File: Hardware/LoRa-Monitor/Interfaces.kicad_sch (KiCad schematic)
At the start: 37 parts, among them Q1 ZXTN25100DFH, Q2 ZXTN25100DFH, Q3 ZXTN25100DFH, Q4 ZXTN25100DFH, Q5 ZXTN25100DFH, Q6 ZXTN25100DFH, U1 ACPL-M61L, U2 ACPL-M61L, U3 ACPL-M61L, U4 MAX3483, U5 ACPL-M61L, U6 ACPL-M61L, U7 ACPL-M61L

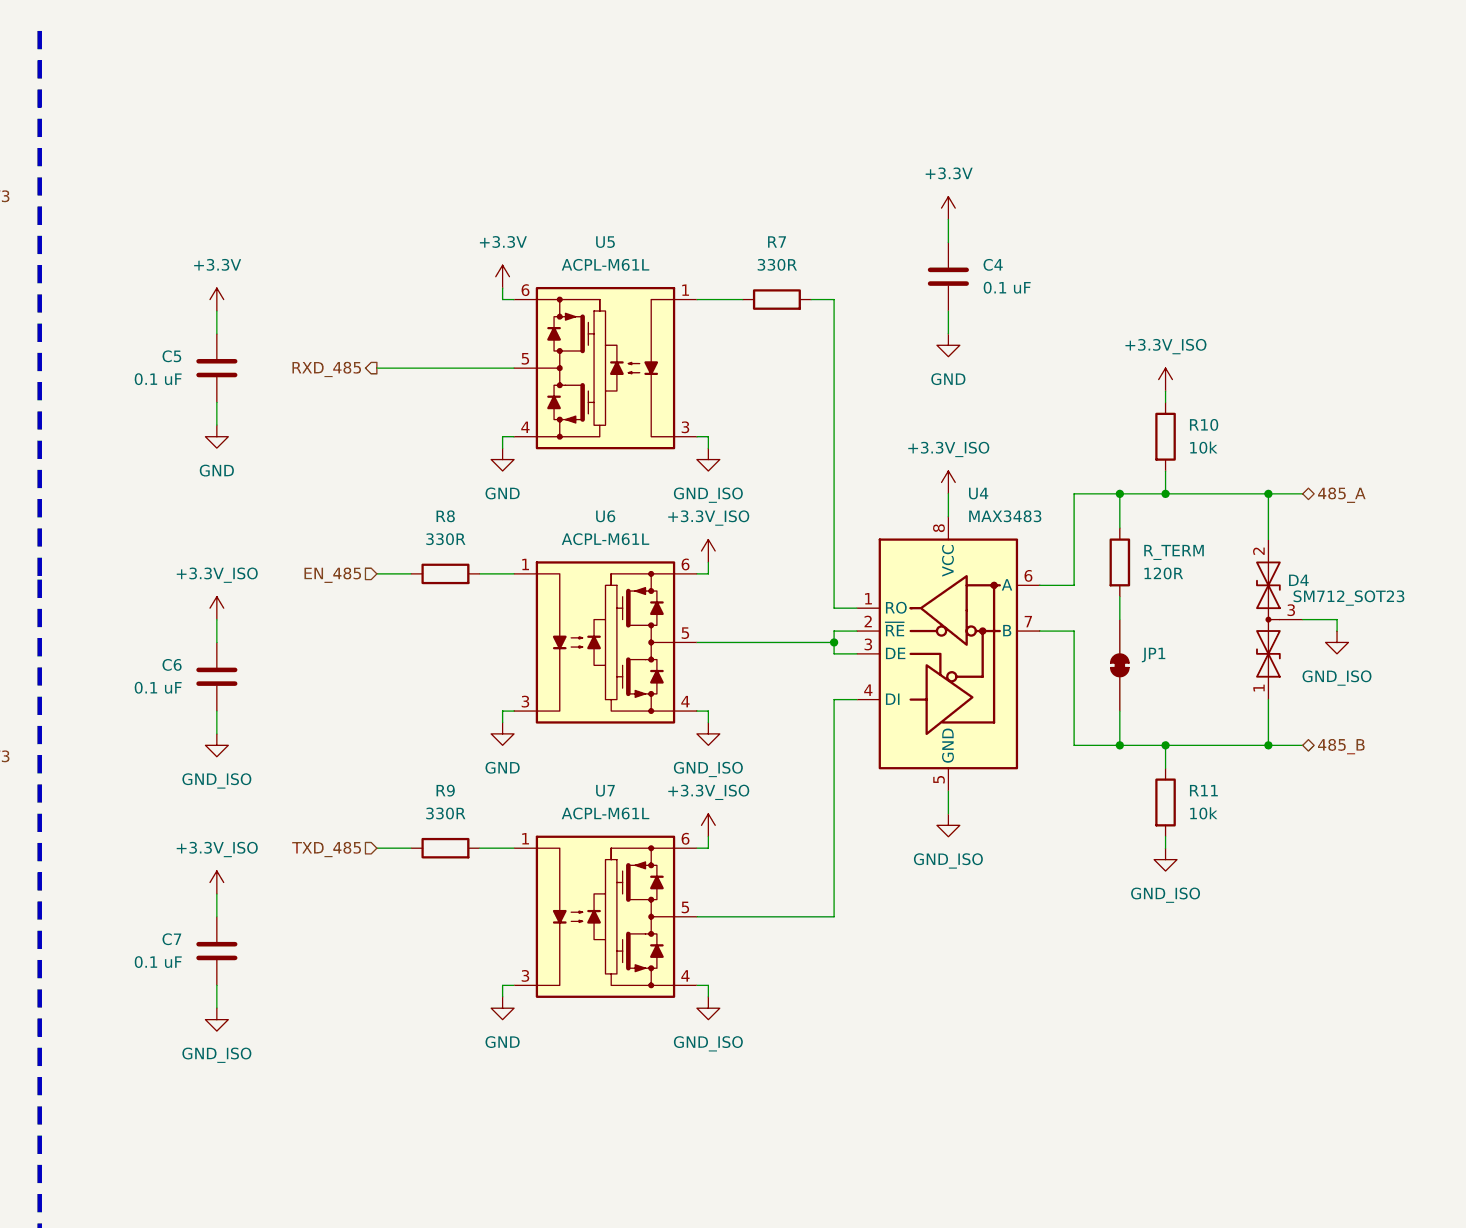
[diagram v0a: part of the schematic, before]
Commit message: Fixed Power and Ground on the Interface nodes
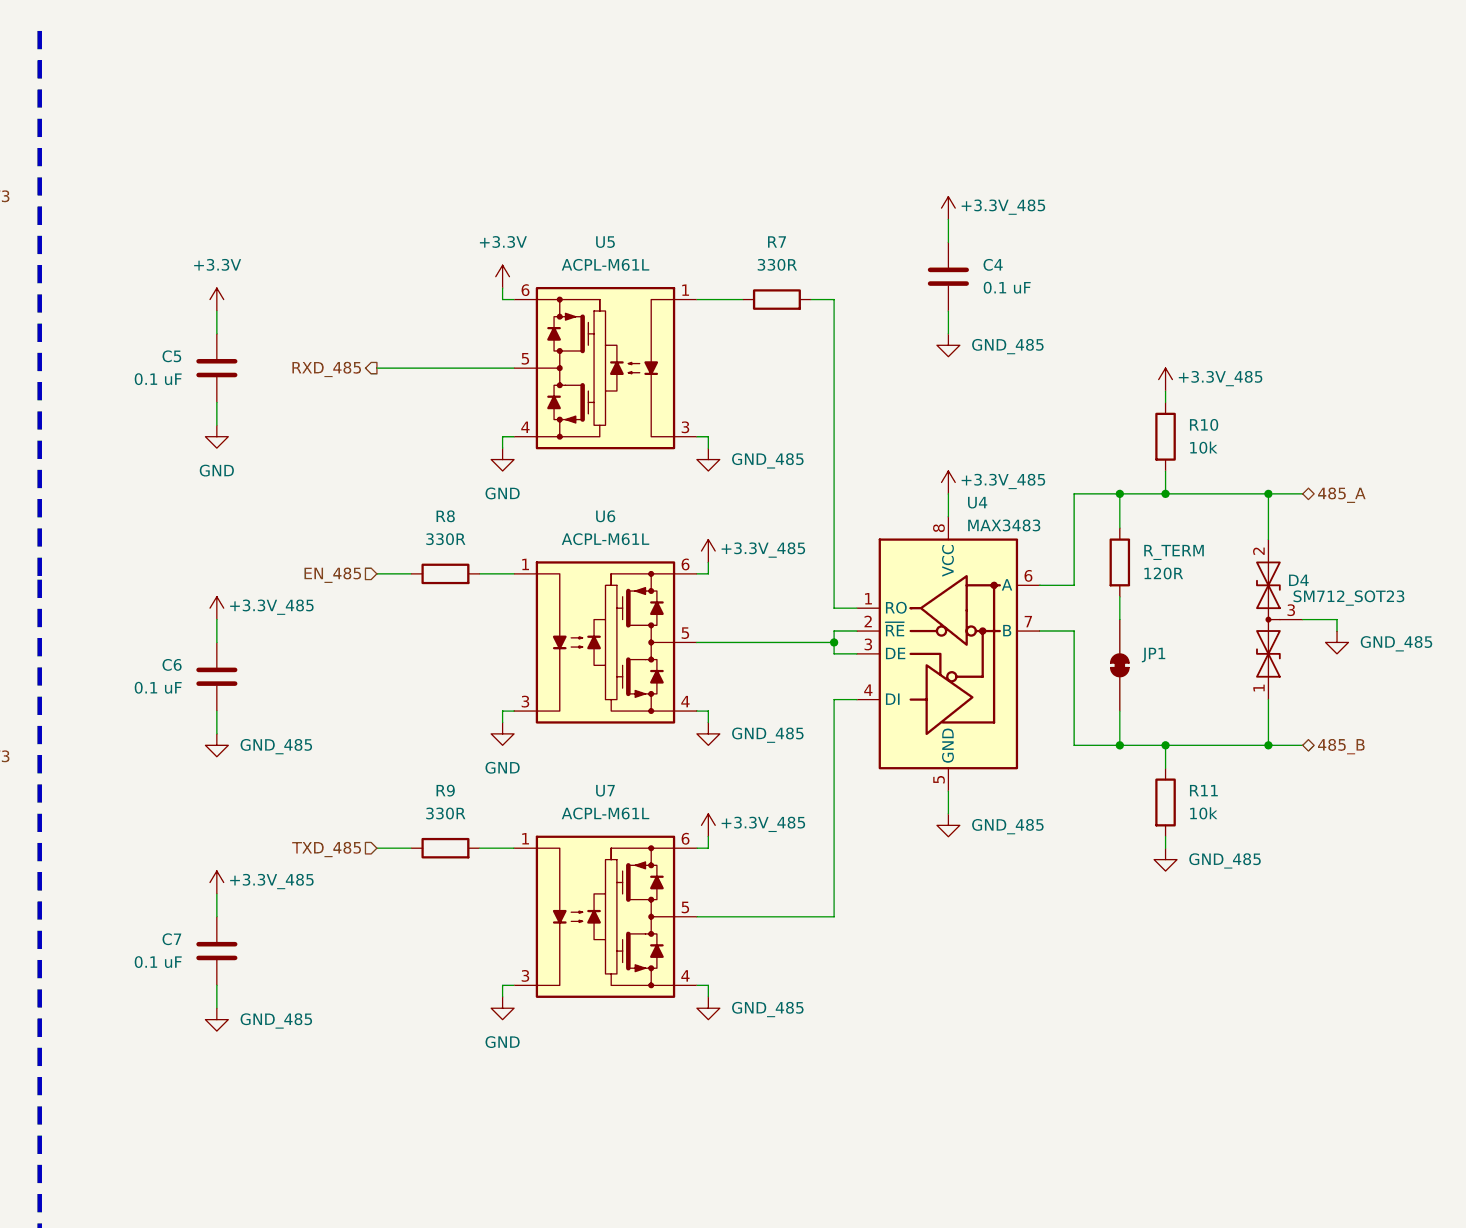
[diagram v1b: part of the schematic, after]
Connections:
- net +3.3V: no longer C4.1
- net GND: no longer C4.2
- net +3.3V_ISO renamed +3.3V_485
- net +3.3V_485: now also C4.1
- net GND_ISO renamed GND_485
- net GND_485: now also C4.2

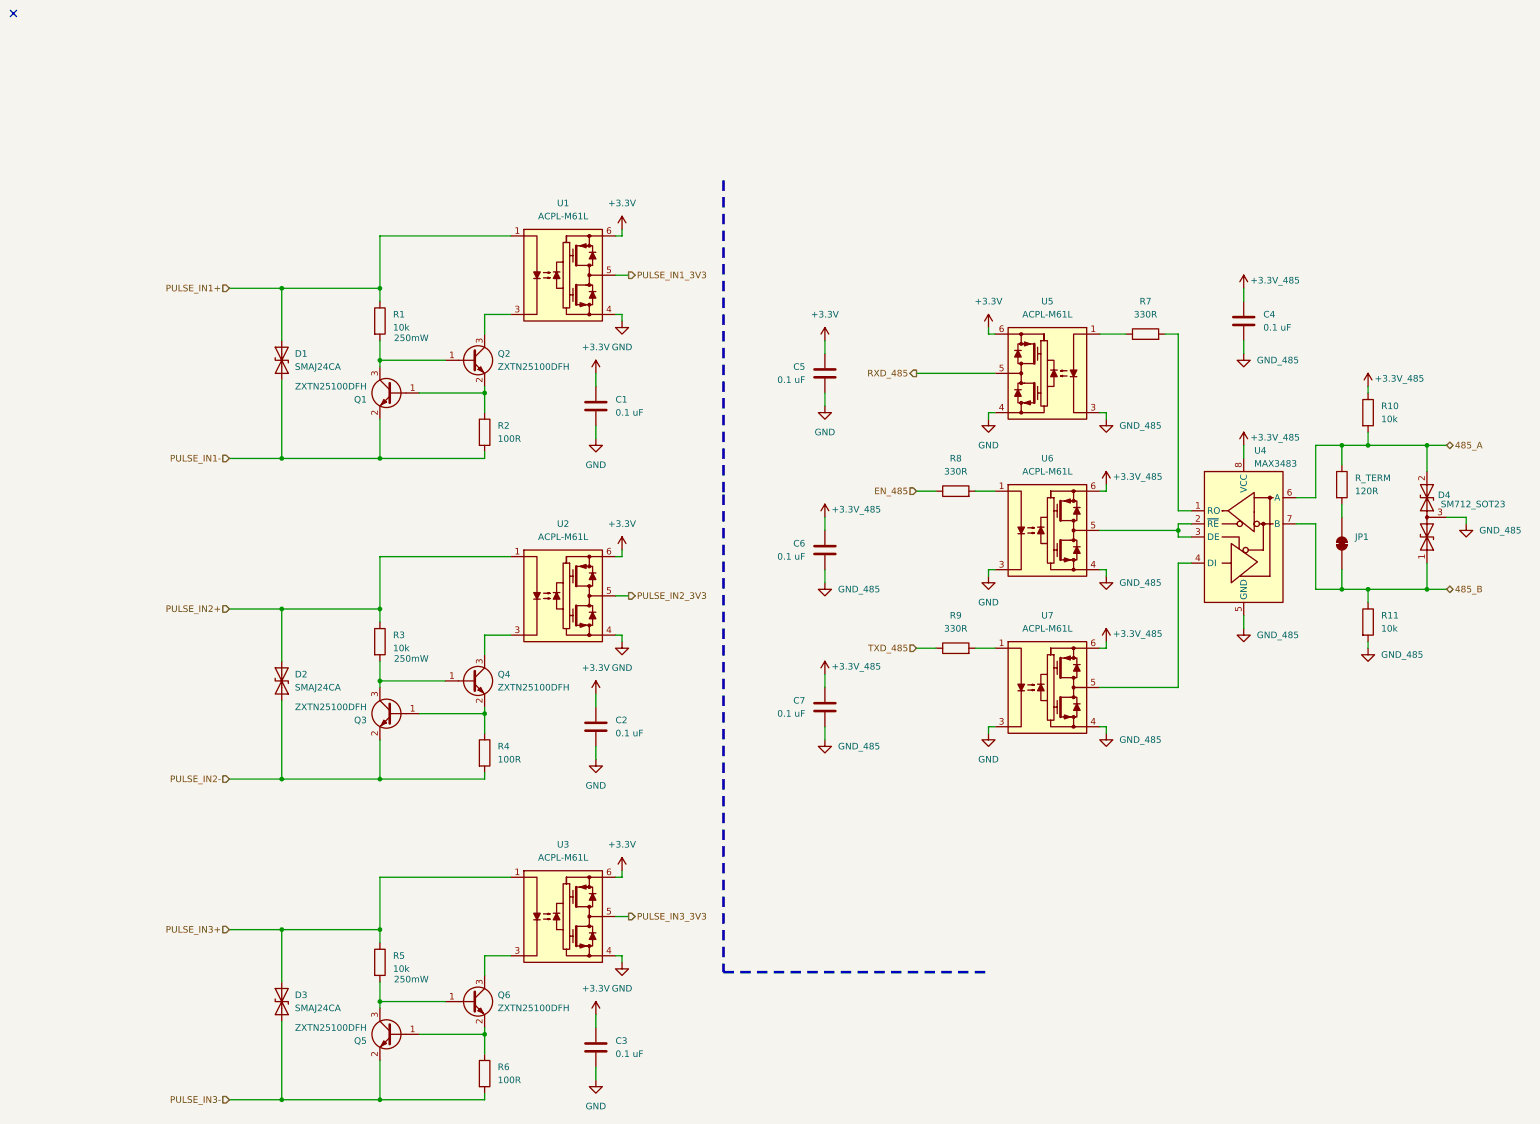
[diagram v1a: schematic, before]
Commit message: Added PSU
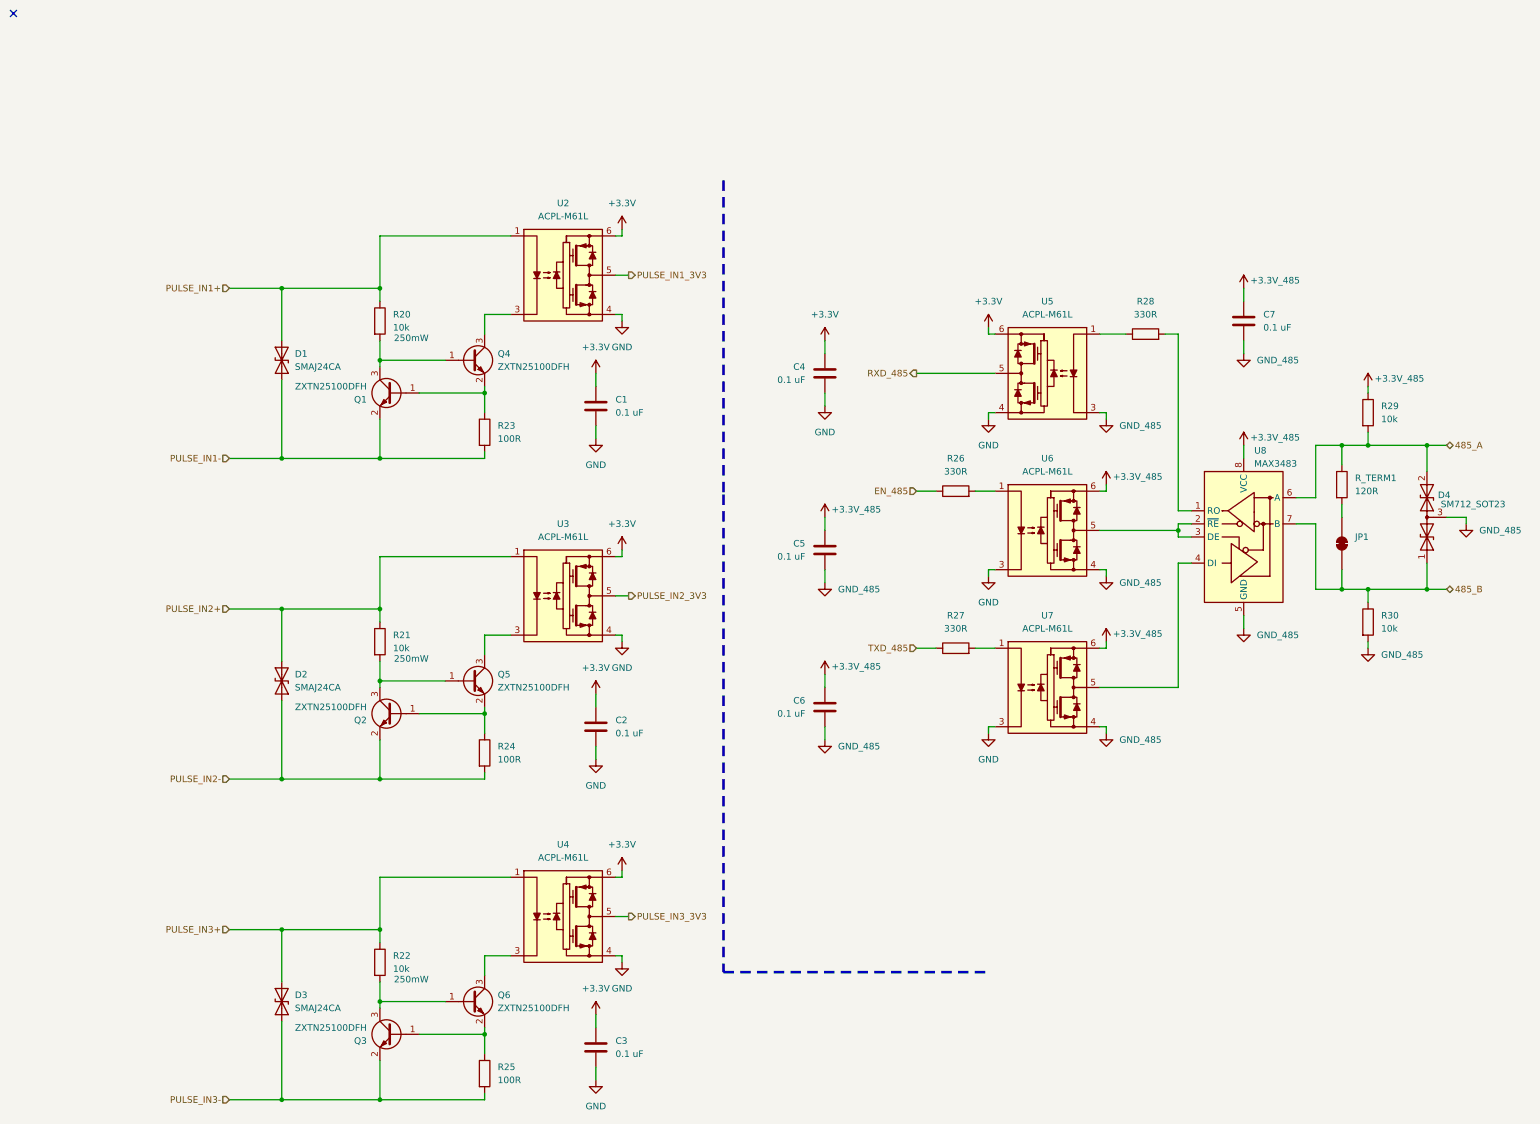
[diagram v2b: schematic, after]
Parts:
- renumbered C5 to C4, C6 to C5, C7 to C6, C4 to C7, Q3 to Q2, Q5 to Q3, Q2 to Q4, Q4 to Q5, R1 to R20, R3 to R21, R5 to R22, R2 to R23, R4 to R24, R6 to R25, R8 to R26, R9 to R27, R7 to R28, R10 to R29, R11 to R30, R_TERM to R_TERM1, U1 to U2, U2 to U3, U3 to U4, U4 to U8

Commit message: Finished PSU module, started Energy meter
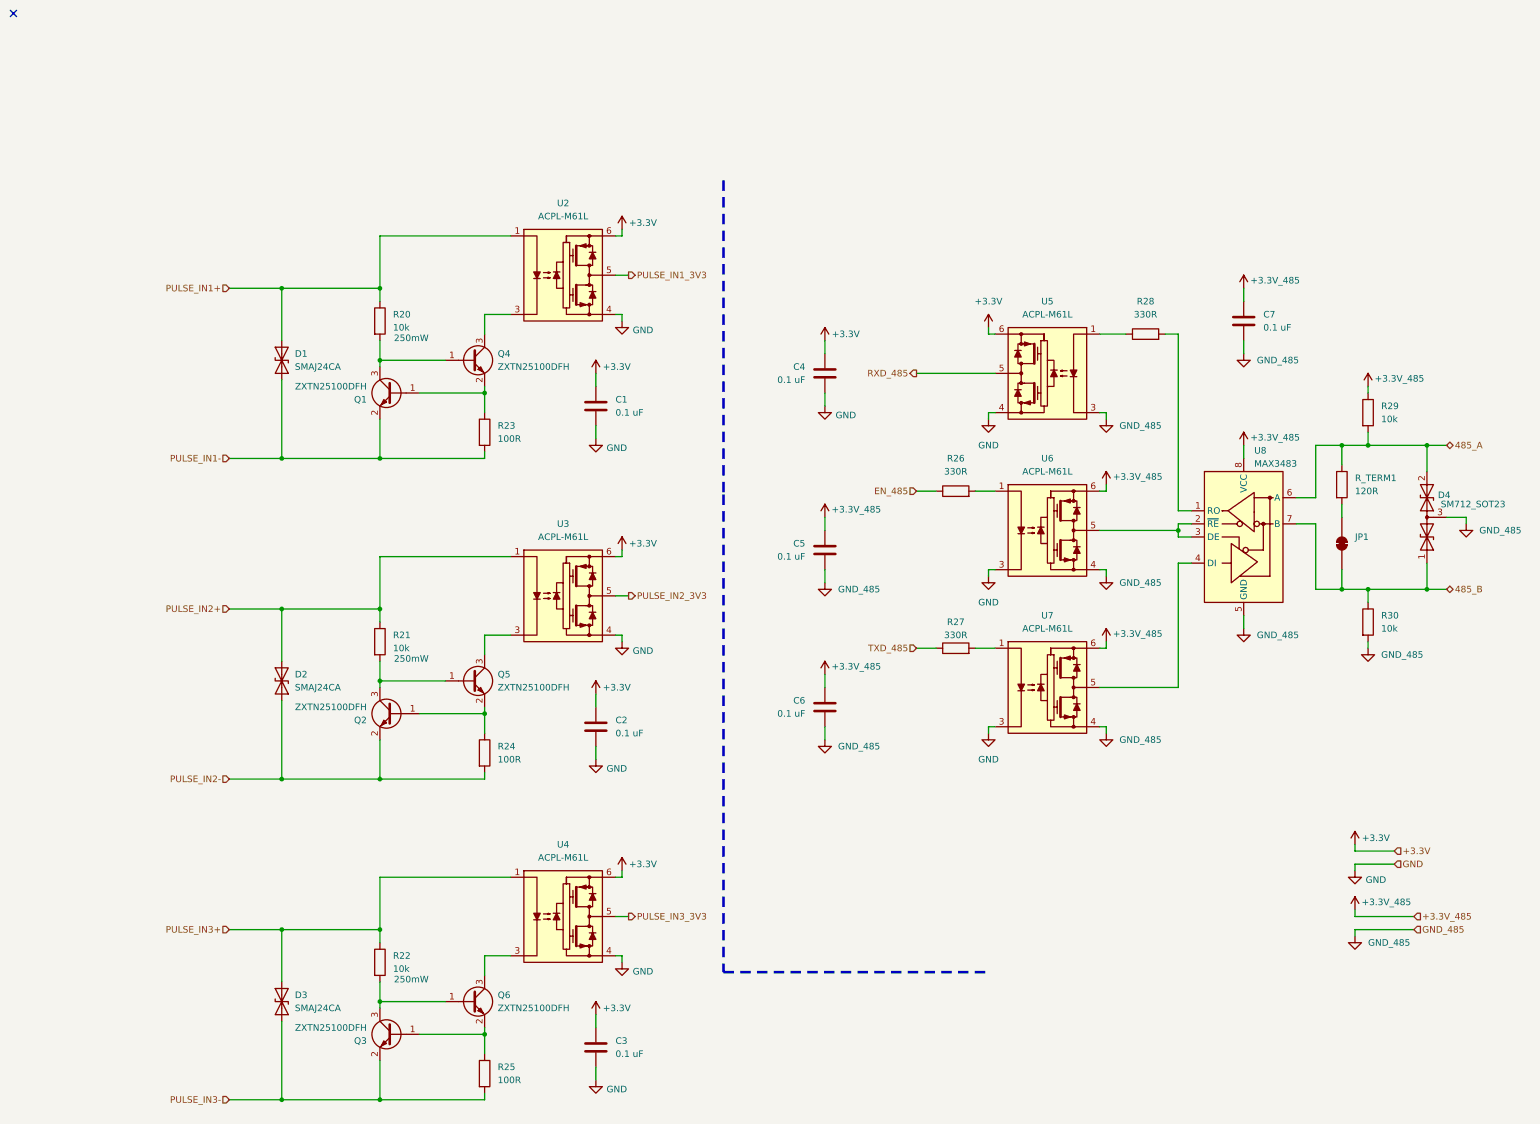
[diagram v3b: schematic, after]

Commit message: Finished schematic, started with PCB design
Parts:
- removed R21: 10k, Resistor_SMD:R_1206_3216Metric, symbol Device:R
- added R102: 10k, Resistor_SMD:R_1206_3216Metric, symbol Device:R
- U2, U3, U4, U5, U6, U7: footprint Package_SO:SO-5-6_4.55x3.7mm_P1.27mm -> DeviceComponents:SO-5_4.39x3.84mm_P1.27mm
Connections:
- net PULSE_IN2+: now also R102.1
- net at Q2.3 (C), Q5.1 (B): now also R102.2
- no-connect marks 1 -> 0

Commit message: Started routing.
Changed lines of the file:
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@@
 	)
 	(junction
-		(at 200.66 72.39)
-		(diameter 0)
-		(color 0 0 0 0)
-	)
-	(junction
 		(at 40.64 157.48)
 		(diameter 0)
@@
 					(unit 1)
 				)
-			)
-		)
-	)
-	(symbol
-		(lib_id "power:PWR_FLAG")
-		(at 200.66 72.39 270)
-		(unit 1)
-		(body_style 1)
-		(exclude_from_sim no)
-		(in_bom yes)
-		(on_board yes)
-		(in_pos_files yes)
-		(dnp no)
-		(fields_autoplaced yes)
-		(property "Reference" "#FLG04"
-			(at 202.565 72.39 0)
-			(hide yes)
-			(show_name no)
-			(do_not_autoplace no)
-			(effects
-				(font
-					(size 1.27 1.27)
-				)
-			)
-		)
-		(property "Value" "PWR_FLAG"
-			(at 204.47 72.3899 90)
-			(show_name no)
-			(do_not_autoplace no)
-			(effects
-				(font
-					(size 1.27 1.27)
-				)
-				(justify left)
-			)
-		)
-		(property "Footprint" ""
-			(at 200.66 72.39 0)
-			(hide yes)
-			(show_name no)
-			(do_not_autoplace no)
-			(effects
-				(font
-					(size 1.27 1.27)
-				)
-			)
-		)
-		(property "Datasheet" ""
-			(at 200.66 72.39 0)
-			(hide yes)
-			(show_name no)
-			(do_not_autoplace no)
-			(effects
-				(font
-					(size 1.27 1.27)
-				)
-			)
-		)
-		(property "Description" "Special symbol for telling ERC where power comes from"
-			(at 200.66 72.39 0)
-			(hide yes)
-			(show_name no)
-			(do_not_autoplace no)
-			(effects
-				(font
-					(size 1.27 1.27)
-				)
-			)
-		)
-		(pin "1"
-		)
-		(instances
-			(project "LoRa-Monitor"
-				(path "/7510cc7d-c141-46d4-8947-7def3af8cf35/eb9302a5-57ee-4bcb-97a3-49e9548a58ec"
-					(reference "#FLG04")
-					(unit 1)
-				)
